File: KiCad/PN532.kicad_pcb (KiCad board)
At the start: 2 copper layers, 42 x 42 mm, 54 parts, among them J1 Bell, J2 Header, J3 SPOX, SW1 TAMPER, U1 PN532, U2 QR, Y1 27.12MHz

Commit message: Tidy
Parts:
- C1, C2: value 200pF -> 180pF
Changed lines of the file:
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@@
       (effects (font (size 0.5 0.5) (thickness 0.08)))
     )
-    (fp_text value 200pF (at 0 0.5) (layer F.Fab)
+    (fp_text value 180pF (at 0 0.5) (layer F.Fab)
       (effects (font (size 0.4 0.4) (thickness 0.08)))
     )
@@
       (effects (font (size 0.4 0.4) (thickness 0.06)))
     )
+    (fp_line (start -0.8 -0.2) (end -0.8 -1) (layer F.Fab) (width 0.1))
+    (fp_line (start -0.8 -1) (end 0.8 -1) (layer F.Fab) (width 0.1))
+    (fp_line (start 0.8 -1) (end 0.8 -0.2) (layer F.Fab) (width 0.1))
+    (fp_line (start 0.8 -0.2) (end -0.8 -0.2) (layer F.Fab) (width 0.1))
+    (fp_line (start -0.14058 -1.11) (end 0.14058 -1.11) (layer F.SilkS) (width 0.12))
+    (fp_line (start -0.14058 -0.09) (end 0.14058 -0.09) (layer F.SilkS) (width 0.12))
+    (fp_line (start -0.8 -0.2) (end -0.8 -1) (layer F.CrtYd) (width 0.05))
+    (fp_line (start -0.8 -1) (end 0.8 -1) (layer F.CrtYd) (width 0.05))
+    (fp_line (start 0.8 -1) (end 0.8 -0.2) (layer F.CrtYd) (width 0.05))
+    (fp_line (start 0.8 -0.2) (end -0.8 -0.2) (layer F.CrtYd) (width 0.05))
+    (fp_line (start -0.8 1) (end -0.8 0.2) (layer F.Fab) (width 0.1))
+    (fp_line (start -0.8 0.2) (end 0.8 0.2) (layer F.Fab) (width 0.1))
+    (fp_line (start 0.8 0.2) (end 0.8 1) (layer F.Fab) (width 0.1))
+    (fp_line (start 0.8 1) (end -0.8 1) (layer F.Fab) (width 0.1))
+    (fp_line (start -0.14058 0.09) (end 0.14058 0.09) (layer F.SilkS) (width 0.12))
+    (fp_line (start -0.14058 1.11) (end 0.14058 1.11) (layer F.SilkS) (width 0.12))
+    (fp_line (start -0.8 1) (end -0.8 0.2) (layer F.CrtYd) (width 0.05))
+    (fp_line (start -0.8 0.2) (end 0.8 0.2) (layer F.CrtYd) (width 0.05))
+    (fp_line (start 0.8 0.2) (end 0.8 1) (layer F.CrtYd) (width 0.05))
     (fp_line (start 0.8 1) (end -0.8 1) (layer F.CrtYd) (width 0.05))
-    (fp_line (start 0.8 0.2) (end 0.8 1) (layer F.CrtYd) (width 0.05))
-    (fp_line (start -0.8 0.2) (end 0.8 0.2) (layer F.CrtYd) (width 0.05))
-    (fp_line (start -0.8 1) (end -0.8 0.2) (layer F.CrtYd) (width 0.05))
-    (fp_line (start -0.14058 1.11) (end 0.14058 1.11) (layer F.SilkS) (width 0.12))
-    (fp_line (start -0.14058 0.09) (end 0.14058 0.09) (layer F.SilkS) (width 0.12))
-    (fp_line (start 0.8 1) (end -0.8 1) (layer F.Fab) (width 0.1))
-    (fp_line (start 0.8 0.2) (end 0.8 1) (layer F.Fab) (width 0.1))
-    (fp_line (start -0.8 0.2) (end 0.8 0.2) (layer F.Fab) (width 0.1))
-    (fp_line (start -0.8 1) (end -0.8 0.2) (layer F.Fab) (width 0.1))
-    (fp_line (start 0.8 -0.2) (end -0.8 -0.2) (layer F.CrtYd) (width 0.05))
-    (fp_line (start 0.8 -1) (end 0.8 -0.2) (layer F.CrtYd) (width 0.05))
-    (fp_line (start -0.8 -1) (end 0.8 -1) (layer F.CrtYd) (width 0.05))
-    (fp_line (start -0.8 -0.2) (end -0.8 -1) (layer F.CrtYd) (width 0.05))
-    (fp_line (start -0.14058 -0.09) (end 0.14058 -0.09) (layer F.SilkS) (width 0.12))
-    (fp_line (start -0.14058 -1.11) (end 0.14058 -1.11) (layer F.SilkS) (width 0.12))
-    (fp_line (start 0.8 -0.2) (end -0.8 -0.2) (layer F.Fab) (width 0.1))
-    (fp_line (start 0.8 -1) (end 0.8 -0.2) (layer F.Fab) (width 0.1))
-    (fp_line (start -0.8 -1) (end 0.8 -1) (layer F.Fab) (width 0.1))
-    (fp_line (start -0.8 -0.2) (end -0.8 -1) (layer F.Fab) (width 0.1))
-    (pad 1 smd roundrect (at -0.775 -0.6 180) (size 0.9 0.95) (layers F.Cu F.Paste F.Mask) (roundrect_rratio 0.25)
+    (pad 1 smd roundrect (at -0.775 -0.6 180) (size 0.9 0.95) (layers F.Cu F.Mask) (roundrect_rratio 0.25)
       (net 1 GND))
-    (pad 2 smd roundrect (at 0.775 -0.6 180) (size 0.9 0.95) (layers F.Cu F.Paste F.Mask) (roundrect_rratio 0.25)
+    (pad 2 smd roundrect (at 0.775 -0.6 180) (size 0.9 0.95) (layers F.Cu F.Mask) (roundrect_rratio 0.25)
       (net 31 "Net-(C2-Pad2)"))
     (pad 2 smd roundrect (at 0.775 0.6 180) (size 0.9 0.95) (layers F.Cu F.Paste F.Mask) (roundrect_rratio 0.25)
@@
       (effects (font (size 0.5 0.5) (thickness 0.08)))
     )
-    (fp_text value 200pF (at 0 0.5) (layer F.Fab)
+    (fp_text value 180pF (at 0 0.5) (layer F.Fab)
       (effects (font (size 0.4 0.4) (thickness 0.08)))
     )
@@
       (effects (font (size 0.4 0.4) (thickness 0.06)))
     )
+    (fp_line (start -0.8 -0.2) (end -0.8 -1) (layer F.Fab) (width 0.1))
+    (fp_line (start -0.8 -1) (end 0.8 -1) (layer F.Fab) (width 0.1))
+    (fp_line (start 0.8 -1) (end 0.8 -0.2) (layer F.Fab) (width 0.1))
+    (fp_line (start 0.8 -0.2) (end -0.8 -0.2) (layer F.Fab) (width 0.1))
+    (fp_line (start -0.14058 -1.11) (end 0.14058 -1.11) (layer F.SilkS) (width 0.12))
+    (fp_line (start -0.14058 -0.09) (end 0.14058 -0.09) (layer F.SilkS) (width 0.12))
+    (fp_line (start -0.8 -0.2) (end -0.8 -1) (layer F.CrtYd) (width 0.05))
+    (fp_line (start -0.8 -1) (end 0.8 -1) (layer F.CrtYd) (width 0.05))
+    (fp_line (start 0.8 -1) (end 0.8 -0.2) (layer F.CrtYd) (width 0.05))
+    (fp_line (start 0.8 -0.2) (end -0.8 -0.2) (layer F.CrtYd) (width 0.05))
+    (fp_line (start -0.8 1) (end -0.8 0.2) (layer F.Fab) (width 0.1))
+    (fp_line (start -0.8 0.2) (end 0.8 0.2) (layer F.Fab) (width 0.1))
+    (fp_line (start 0.8 0.2) (end 0.8 1) (layer F.Fab) (width 0.1))
+    (fp_line (start 0.8 1) (end -0.8 1) (layer F.Fab) (width 0.1))
+    (fp_line (start -0.14058 0.09) (end 0.14058 0.09) (layer F.SilkS) (width 0.12))
+    (fp_line (start -0.14058 1.11) (end 0.14058 1.11) (layer F.SilkS) (width 0.12))
+    (fp_line (start -0.8 1) (end -0.8 0.2) (layer F.CrtYd) (width 0.05))
+    (fp_line (start -0.8 0.2) (end 0.8 0.2) (layer F.CrtYd) (width 0.05))
+    (fp_line (start 0.8 0.2) (end 0.8 1) (layer F.CrtYd) (width 0.05))
     (fp_line (start 0.8 1) (end -0.8 1) (layer F.CrtYd) (width 0.05))
-    (fp_line (start 0.8 0.2) (end 0.8 1) (layer F.CrtYd) (width 0.05))
-    (fp_line (start -0.8 0.2) (end 0.8 0.2) (layer F.CrtYd) (width 0.05))
-    (fp_line (start -0.8 1) (end -0.8 0.2) (layer F.CrtYd) (width 0.05))
-    (fp_line (start -0.14058 1.11) (end 0.14058 1.11) (layer F.SilkS) (width 0.12))
-    (fp_line (start -0.14058 0.09) (end 0.14058 0.09) (layer F.SilkS) (width 0.12))
-    (fp_line (start 0.8 1) (end -0.8 1) (layer F.Fab) (width 0.1))
-    (fp_line (start 0.8 0.2) (end 0.8 1) (layer F.Fab) (width 0.1))
-    (fp_line (start -0.8 0.2) (end 0.8 0.2) (layer F.Fab) (width 0.1))
-    (fp_line (start -0.8 1) (end -0.8 0.2) (layer F.Fab) (width 0.1))
-    (fp_line (start 0.8 -0.2) (end -0.8 -0.2) (layer F.CrtYd) (width 0.05))
-    (fp_line (start 0.8 -1) (end 0.8 -0.2) (layer F.CrtYd) (width 0.05))
-    (fp_line (start -0.8 -1) (end 0.8 -1) (layer F.CrtYd) (width 0.05))
-    (fp_line (start -0.8 -0.2) (end -0.8 -1) (layer F.CrtYd) (width 0.05))
-    (fp_line (start -0.14058 -0.09) (end 0.14058 -0.09) (layer F.SilkS) (width 0.12))
-    (fp_line (start -0.14058 -1.11) (end 0.14058 -1.11) (layer F.SilkS) (width 0.12))
-    (fp_line (start 0.8 -0.2) (end -0.8 -0.2) (layer F.Fab) (width 0.1))
-    (fp_line (start 0.8 -1) (end 0.8 -0.2) (layer F.Fab) (width 0.1))
-    (fp_line (start -0.8 -1) (end 0.8 -1) (layer F.Fab) (width 0.1))
-    (fp_line (start -0.8 -0.2) (end -0.8 -1) (layer F.Fab) (width 0.1))
-    (pad 1 smd roundrect (at -0.775 -0.6 180) (size 0.9 0.95) (layers F.Cu F.Paste F.Mask) (roundrect_rratio 0.25)
+    (pad 1 smd roundrect (at -0.775 -0.6 180) (size 0.9 0.95) (layers F.Cu F.Mask) (roundrect_rratio 0.25)
       (net 30 "Net-(C1-Pad1)"))
-    (pad 2 smd roundrect (at 0.775 -0.6 180) (size 0.9 0.95) (layers F.Cu F.Paste F.Mask) (roundrect_rratio 0.25)
+    (pad 2 smd roundrect (at 0.775 -0.6 180) (size 0.9 0.95) (layers F.Cu F.Mask) (roundrect_rratio 0.25)
       (net 1 GND))
     (pad 2 smd roundrect (at 0.775 0.6 180) (size 0.9 0.95) (layers F.Cu F.Paste F.Mask) (roundrect_rratio 0.25)

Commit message: Final tidy for order
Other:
- board text added: "2021-05-17"
- board text removed: "2021-05-13"
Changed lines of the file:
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@@
     (34 B.Paste user hide)
     (35 F.Paste user hide)
-    (36 B.SilkS user hide)
-    (37 F.SilkS user hide)
+    (36 B.SilkS user)
+    (37 F.SilkS user)
     (38 B.Mask user hide)
     (39 F.Mask user hide)
@@
     (tags "CONN DEV")
     (attr virtual)
-    (fp_text reference J1 (at 1.3 2 90) (layer B.SilkS)
+    (fp_text reference J1 (at 1.3 2 90) (layer B.SilkS) hide
       (effects (font (size 1 1) (thickness 0.15)) (justify mirror))
     )
@@
       (effects (font (size 0.4 0.4) (thickness 0.06)))
     )
-    (fp_line (start -0.8 -0.2) (end -0.8 -1) (layer F.Fab) (width 0.1))
-    (fp_line (start -0.8 -1) (end 0.8 -1) (layer F.Fab) (width 0.1))
-    (fp_line (start 0.8 -1) (end 0.8 -0.2) (layer F.Fab) (width 0.1))
-    (fp_line (start 0.8 -0.2) (end -0.8 -0.2) (layer F.Fab) (width 0.1))
-    (fp_line (start -0.14058 -1.11) (end 0.14058 -1.11) (layer F.SilkS) (width 0.12))
-    (fp_line (start -0.14058 -0.09) (end 0.14058 -0.09) (layer F.SilkS) (width 0.12))
-    (fp_line (start -0.8 -0.2) (end -0.8 -1) (layer F.CrtYd) (width 0.05))
-    (fp_line (start -0.8 -1) (end 0.8 -1) (layer F.CrtYd) (width 0.05))
-    (fp_line (start 0.8 -1) (end 0.8 -0.2) (layer F.CrtYd) (width 0.05))
-    (fp_line (start 0.8 -0.2) (end -0.8 -0.2) (layer F.CrtYd) (width 0.05))
-    (fp_line (start -0.8 1) (end -0.8 0.2) (layer F.Fab) (width 0.1))
-    (fp_line (start -0.8 0.2) (end 0.8 0.2) (layer F.Fab) (width 0.1))
-    (fp_line (start 0.8 0.2) (end 0.8 1) (layer F.Fab) (width 0.1))
-    (fp_line (start 0.8 1) (end -0.8 1) (layer F.Fab) (width 0.1))
-    (fp_line (start -0.14058 0.09) (end 0.14058 0.09) (layer F.SilkS) (width 0.12))
-    (fp_line (start -0.14058 1.11) (end 0.14058 1.11) (layer F.SilkS) (width 0.12))
-    (fp_line (start -0.8 1) (end -0.8 0.2) (layer F.CrtYd) (width 0.05))
-    (fp_line (start -0.8 0.2) (end 0.8 0.2) (layer F.CrtYd) (width 0.05))
-    (fp_line (start 0.8 0.2) (end 0.8 1) (layer F.CrtYd) (width 0.05))
     (fp_line (start 0.8 1) (end -0.8 1) (layer F.CrtYd) (width 0.05))
-    (pad 1 smd roundrect (at -0.775 -0.6 180) (size 0.9 0.95) (layers F.Cu F.Mask) (roundrect_rratio 0.25)
+    (fp_line (start 0.8 0.2) (end 0.8 1) (layer F.CrtYd) (width 0.05))
+    (fp_line (start -0.8 0.2) (end 0.8 0.2) (layer F.CrtYd) (width 0.05))
+    (fp_line (start -0.8 1) (end -0.8 0.2) (layer F.CrtYd) (width 0.05))
+    (fp_line (start -0.14058 1.11) (end 0.14058 1.11) (layer F.SilkS) (width 0.12))
+    (fp_line (start -0.14058 0.09) (end 0.14058 0.09) (layer F.SilkS) (width 0.12))
+    (fp_line (start 0.8 1) (end -0.8 1) (layer F.Fab) (width 0.1))
+    (fp_line (start 0.8 0.2) (end 0.8 1) (layer F.Fab) (width 0.1))
+    (fp_line (start -0.8 0.2) (end 0.8 0.2) (layer F.Fab) (width 0.1))
+    (fp_line (start -0.8 1) (end -0.8 0.2) (layer F.Fab) (width 0.1))
+    (fp_line (start 0.8 -0.2) (end -0.8 -0.2) (layer F.CrtYd) (width 0.05))
+    (fp_line (start 0.8 -1) (end 0.8 -0.2) (layer F.CrtYd) (width 0.05))
+    (fp_line (start -0.8 -1) (end 0.8 -1) (layer F.CrtYd) (width 0.05))
+    (fp_line (start -0.8 -0.2) (end -0.8 -1) (layer F.CrtYd) (width 0.05))
+    (fp_line (start -0.14058 -0.09) (end 0.14058 -0.09) (layer F.SilkS) (width 0.12))
+    (fp_line (start -0.14058 -1.11) (end 0.14058 -1.11) (layer F.SilkS) (width 0.12))
+    (fp_line (start 0.8 -0.2) (end -0.8 -0.2) (layer F.Fab) (width 0.1))
+    (fp_line (start 0.8 -1) (end 0.8 -0.2) (layer F.Fab) (width 0.1))
+    (fp_line (start -0.8 -1) (end 0.8 -1) (layer F.Fab) (width 0.1))
+    (fp_line (start -0.8 -0.2) (end -0.8 -1) (layer F.Fab) (width 0.1))
+    (pad 1 smd roundrect (at -0.775 -0.6 180) (size 0.9 0.95) (layers F.Cu F.Paste F.Mask) (roundrect_rratio 0.25)
       (net 1 GND))
-    (pad 2 smd roundrect (at 0.775 -0.6 180) (size 0.9 0.95) (layers F.Cu F.Mask) (roundrect_rratio 0.25)
+    (pad 2 smd roundrect (at 0.775 -0.6 180) (size 0.9 0.95) (layers F.Cu F.Paste F.Mask) (roundrect_rratio 0.25)
       (net 31 "Net-(C2-Pad2)"))
-    (pad 2 smd roundrect (at 0.775 0.6 180) (size 0.9 0.95) (layers F.Cu F.Paste F.Mask) (roundrect_rratio 0.25)
+    (pad 2 smd roundrect (at 0.775 0.6 180) (size 0.9 0.95) (layers F.Cu F.Mask) (roundrect_rratio 0.25)
       (net 31 "Net-(C2-Pad2)"))
-    (pad 1 smd roundrect (at -0.775 0.6 180) (size 0.9 0.95) (layers F.Cu F.Paste F.Mask) (roundrect_rratio 0.25)
+    (pad 1 smd roundrect (at -0.775 0.6 180) (size 0.9 0.95) (layers F.Cu F.Mask) (roundrect_rratio 0.25)
       (net 1 GND))
     (model ${KISYS3DMOD}/Capacitor_SMD.3dshapes/C_0603_1608Metric.wrl
@@
       (effects (font (size 0.4 0.4) (thickness 0.06)))
     )
-    (fp_line (start -0.8 -0.2) (end -0.8 -1) (layer F.Fab) (width 0.1))
-    (fp_line (start -0.8 -1) (end 0.8 -1) (layer F.Fab) (width 0.1))
-    (fp_line (start 0.8 -1) (end 0.8 -0.2) (layer F.Fab) (width 0.1))
-    (fp_line (start 0.8 -0.2) (end -0.8 -0.2) (layer F.Fab) (width 0.1))
-    (fp_line (start -0.14058 -1.11) (end 0.14058 -1.11) (layer F.SilkS) (width 0.12))
-    (fp_line (start -0.14058 -0.09) (end 0.14058 -0.09) (layer F.SilkS) (width 0.12))
-    (fp_line (start -0.8 -0.2) (end -0.8 -1) (layer F.CrtYd) (width 0.05))
-    (fp_line (start -0.8 -1) (end 0.8 -1) (layer F.CrtYd) (width 0.05))
-    (fp_line (start 0.8 -1) (end 0.8 -0.2) (layer F.CrtYd) (width 0.05))
-    (fp_line (start 0.8 -0.2) (end -0.8 -0.2) (layer F.CrtYd) (width 0.05))
-    (fp_line (start -0.8 1) (end -0.8 0.2) (layer F.Fab) (width 0.1))
-    (fp_line (start -0.8 0.2) (end 0.8 0.2) (layer F.Fab) (width 0.1))
-    (fp_line (start 0.8 0.2) (end 0.8 1) (layer F.Fab) (width 0.1))
-    (fp_line (start 0.8 1) (end -0.8 1) (layer F.Fab) (width 0.1))
-    (fp_line (start -0.14058 0.09) (end 0.14058 0.09) (layer F.SilkS) (width 0.12))
-    (fp_line (start -0.14058 1.11) (end 0.14058 1.11) (layer F.SilkS) (width 0.12))
-    (fp_line (start -0.8 1) (end -0.8 0.2) (layer F.CrtYd) (width 0.05))
-    (fp_line (start -0.8 0.2) (end 0.8 0.2) (layer F.CrtYd) (width 0.05))
-    (fp_line (start 0.8 0.2) (end 0.8 1) (layer F.CrtYd) (width 0.05))
     (fp_line (start 0.8 1) (end -0.8 1) (layer F.CrtYd) (width 0.05))
-    (pad 1 smd roundrect (at -0.775 -0.6 180) (size 0.9 0.95) (layers F.Cu F.Mask) (roundrect_rratio 0.25)
+    (fp_line (start 0.8 0.2) (end 0.8 1) (layer F.CrtYd) (width 0.05))
+    (fp_line (start -0.8 0.2) (end 0.8 0.2) (layer F.CrtYd) (width 0.05))
+    (fp_line (start -0.8 1) (end -0.8 0.2) (layer F.CrtYd) (width 0.05))
+    (fp_line (start -0.14058 1.11) (end 0.14058 1.11) (layer F.SilkS) (width 0.12))
+    (fp_line (start -0.14058 0.09) (end 0.14058 0.09) (layer F.SilkS) (width 0.12))
+    (fp_line (start 0.8 1) (end -0.8 1) (layer F.Fab) (width 0.1))
+    (fp_line (start 0.8 0.2) (end 0.8 1) (layer F.Fab) (width 0.1))
+    (fp_line (start -0.8 0.2) (end 0.8 0.2) (layer F.Fab) (width 0.1))
+    (fp_line (start -0.8 1) (end -0.8 0.2) (layer F.Fab) (width 0.1))
+    (fp_line (start 0.8 -0.2) (end -0.8 -0.2) (layer F.CrtYd) (width 0.05))
+    (fp_line (start 0.8 -1) (end 0.8 -0.2) (layer F.CrtYd) (width 0.05))
+    (fp_line (start -0.8 -1) (end 0.8 -1) (layer F.CrtYd) (width 0.05))
+    (fp_line (start -0.8 -0.2) (end -0.8 -1) (layer F.CrtYd) (width 0.05))
+    (fp_line (start -0.14058 -0.09) (end 0.14058 -0.09) (layer F.SilkS) (width 0.12))
+    (fp_line (start -0.14058 -1.11) (end 0.14058 -1.11) (layer F.SilkS) (width 0.12))
+    (fp_line (start 0.8 -0.2) (end -0.8 -0.2) (layer F.Fab) (width 0.1))
+    (fp_line (start 0.8 -1) (end 0.8 -0.2) (layer F.Fab) (width 0.1))
+    (fp_line (start -0.8 -1) (end 0.8 -1) (layer F.Fab) (width 0.1))
+    (fp_line (start -0.8 -0.2) (end -0.8 -1) (layer F.Fab) (width 0.1))
+    (pad 1 smd roundrect (at -0.775 -0.6 180) (size 0.9 0.95) (layers F.Cu F.Paste F.Mask) (roundrect_rratio 0.25)
       (net 30 "Net-(C1-Pad1)"))
-    (pad 2 smd roundrect (at 0.775 -0.6 180) (size 0.9 0.95) (layers F.Cu F.Mask) (roundrect_rratio 0.25)
+    (pad 2 smd roundrect (at 0.775 -0.6 180) (size 0.9 0.95) (layers F.Cu F.Paste F.Mask) (roundrect_rratio 0.25)
       (net 1 GND))
-    (pad 2 smd roundrect (at 0.775 0.6 180) (size 0.9 0.95) (layers F.Cu F.Paste F.Mask) (roundrect_rratio 0.25)
+    (pad 2 smd roundrect (at 0.775 0.6 180) (size 0.9 0.95) (layers F.Cu F.Mask) (roundrect_rratio 0.25)
       (net 1 GND))
-    (pad 1 smd roundrect (at -0.775 0.6 180) (size 0.9 0.95) (layers F.Cu F.Paste F.Mask) (roundrect_rratio 0.25)
+    (pad 1 smd roundrect (at -0.775 0.6 180) (size 0.9 0.95) (layers F.Cu F.Mask) (roundrect_rratio 0.25)
       (net 30 "Net-(C1-Pad1)"))
     (model ${KISYS3DMOD}/Capacitor_SMD.3dshapes/C_0603_1608Metric.wrl
@@
     (pad 1 thru_hole rect (at 0 0 270) (size 1.7 1.7) (drill 1) (layers *.Cu *.Mask)
       (net 1 GND))
-    (model ${KISYS3DMOD}/Connector_PinHeader_2.54mm.3dshapes/PinHeader_1x04_P2.54mm_Vertical.wrl
-      (at (xyz 0 0 0))
-      (scale (xyz 1 1 1))
-      (rotate (xyz 0 0 0))
-    )
   )
   (module RevK:LED_D3.0mm_and_SMD locked (layer B.Cu)
@@
     (effects (font (size 1 1) (thickness 0.15)))
   )
-  (gr_text 2021-05-13 (at 88 108) (layer F.Cu)
+  (gr_text 2021-05-17 (at 88 108) (layer F.Cu)
     (effects (font (size 0.6 0.6) (thickness 0.1)))
   )

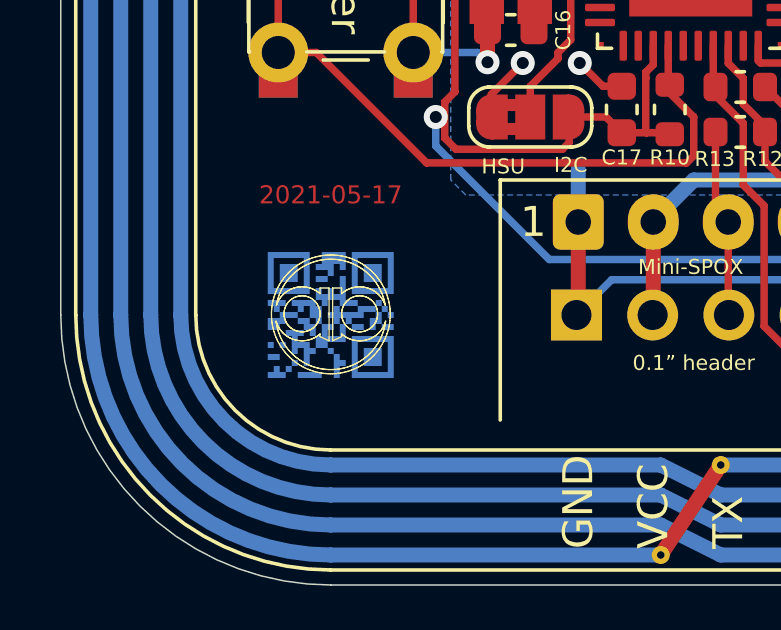
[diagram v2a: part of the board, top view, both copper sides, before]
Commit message: Updated logo on copper
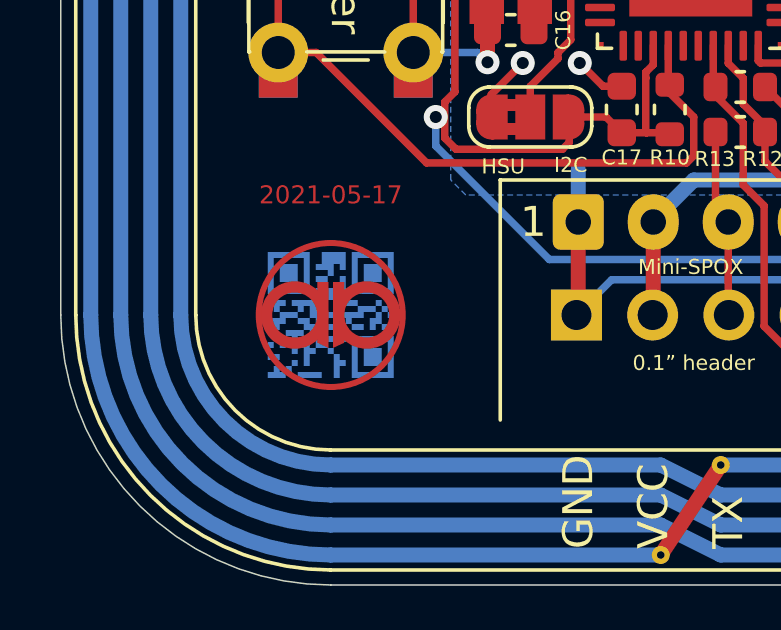
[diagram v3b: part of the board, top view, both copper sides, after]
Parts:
- added 1: AA, RevK:AA, F.Cu at (88.0, 114.4)
- C1, C2: value 180pF -> 172pF

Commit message: A&A logo
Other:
- board text added: "2021-05-18"
- board text removed: "2021-05-17"

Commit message: 200pF
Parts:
- C1, C2: value 172pF -> 200pF
